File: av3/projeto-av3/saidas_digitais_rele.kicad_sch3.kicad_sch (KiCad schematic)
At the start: 0 parts

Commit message: Ligação do cristal no atmega2560 e início do esquemático das saídas digitais com relé.
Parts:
- added D9: 1N4004, Diode_THT:D_DO-41_SOD81_P10.16mm_Horizontal, symbol Diode:1N4004
- added J5: Screw_Terminal_01x03, symbol Connector:Screw_Terminal_01x03
- added K1: Relay_SPDT, symbol Relay:Relay_SPDT
- added Q1: BC337, Package_TO_SOT_THT:TO-92_Inline, symbol Transistor_BJT:BC337
- added R13: R, symbol Device:R
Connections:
- new net: J5.1 (Pin_1), K1.11
- new net: J5.2 (Pin_2), K1.14
- new net: J5.3 (Pin_3), K1.12
- new net: D9.2 (A), K1.A2, Q1.1 (C)
- new net: Q1.2 (B), R13.2
- new net +5V: D9.1 (K), K1.A1
- new net Earth: Q1.3 (E)

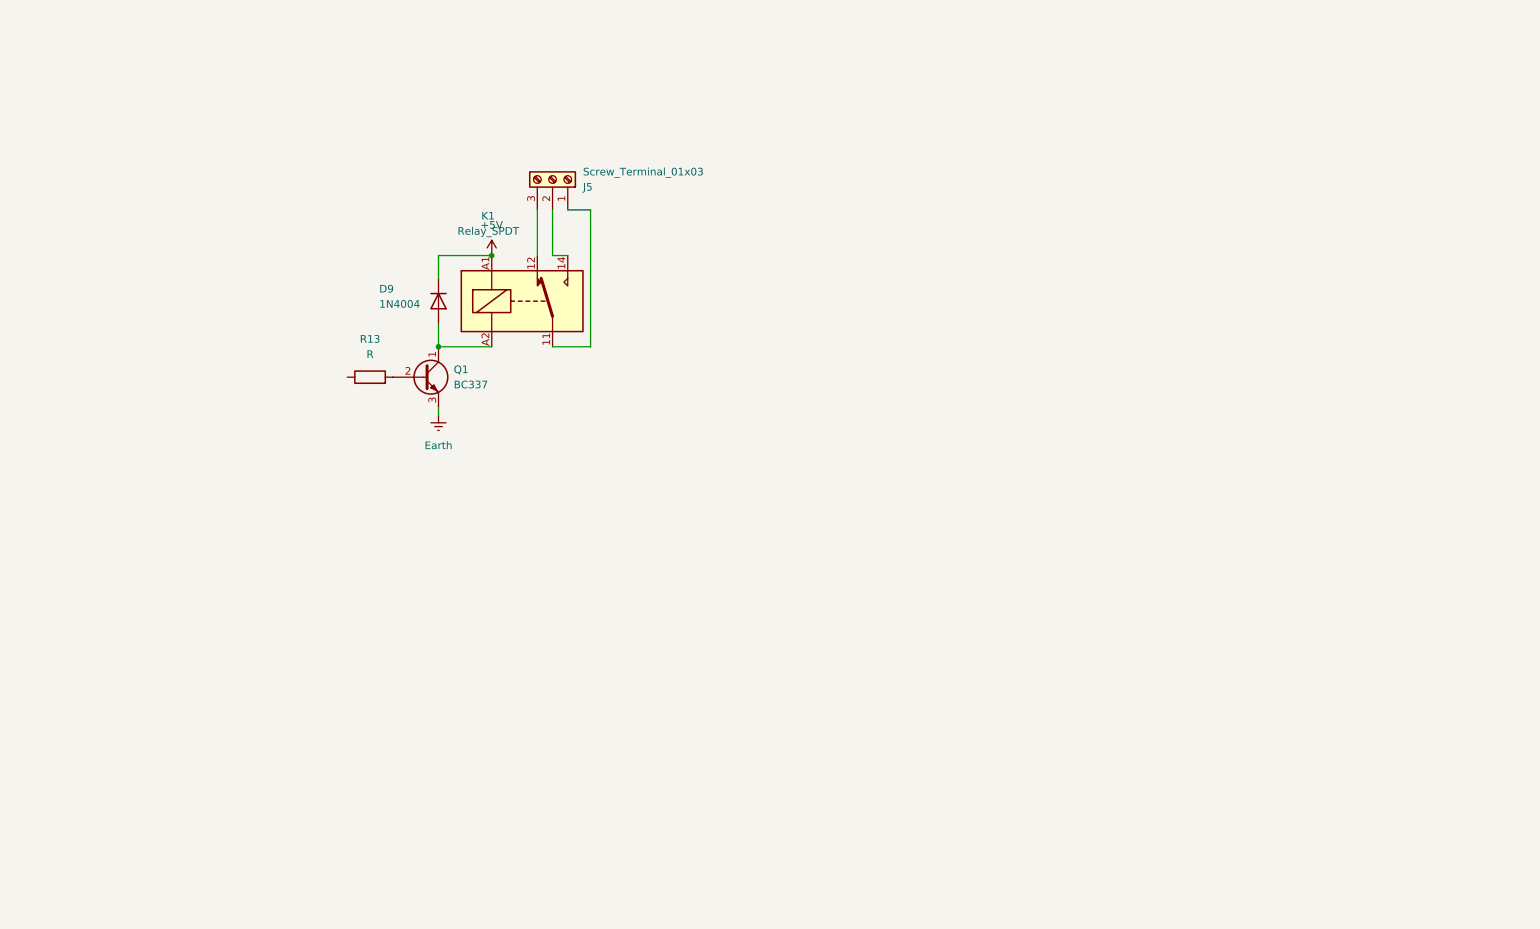
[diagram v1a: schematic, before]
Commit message: Maioria dos esquemáticos finalizados.
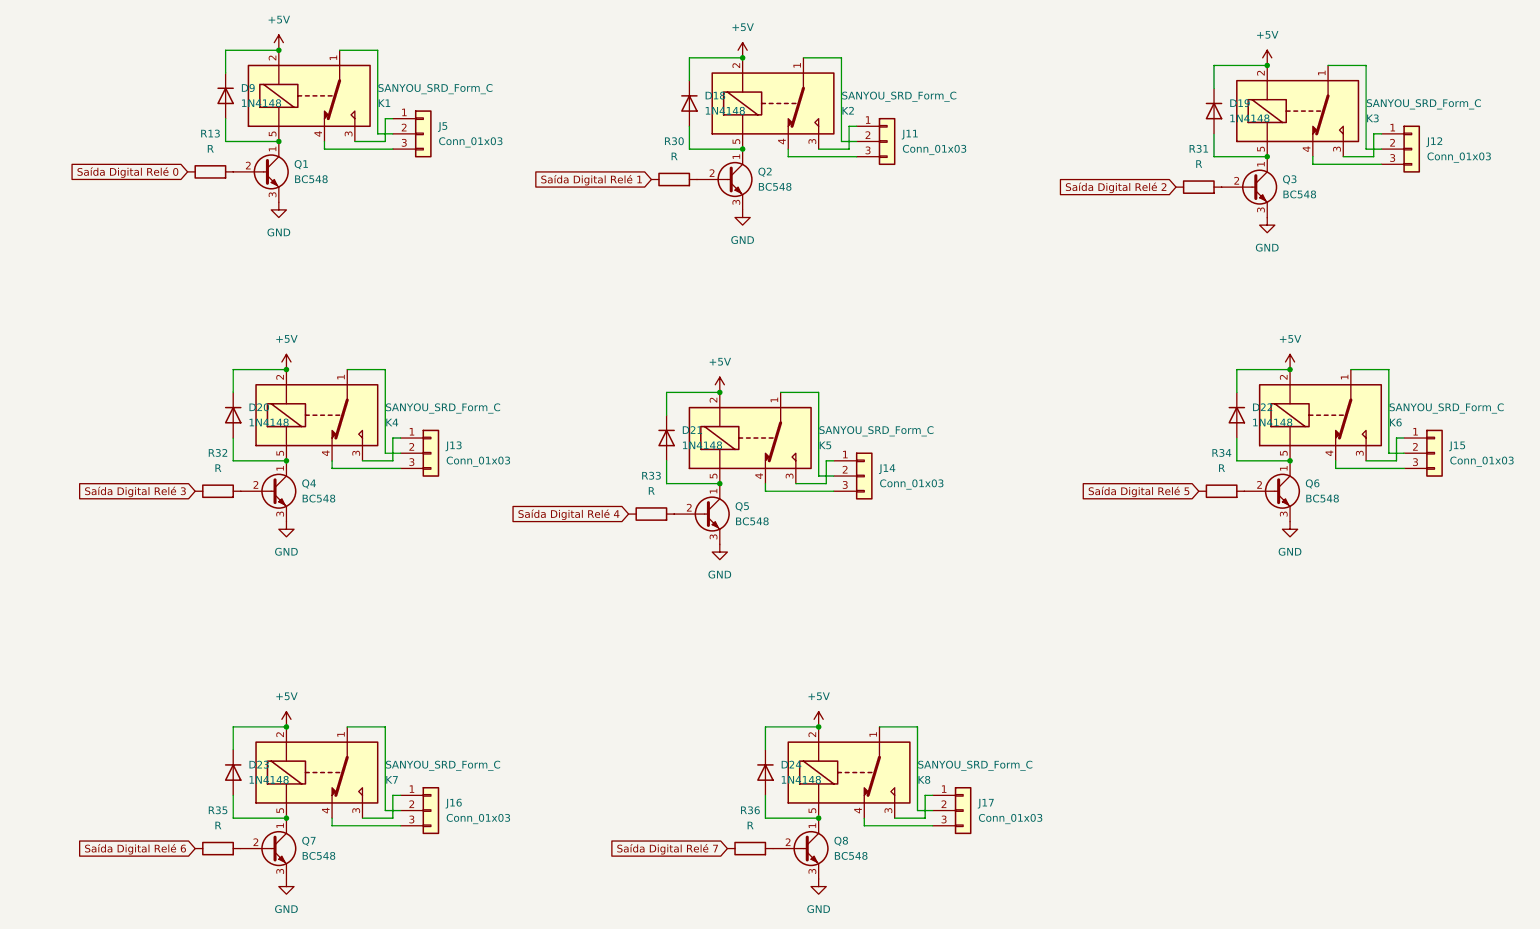
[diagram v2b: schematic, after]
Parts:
- removed D9: 1N4004, Diode_THT:D_DO-41_SOD81_P10.16mm_Horizontal, symbol Diode:1N4004
- removed J5: Screw_Terminal_01x03, symbol Connector:Screw_Terminal_01x03
- removed K1: Relay_SPDT, symbol Relay:Relay_SPDT
- removed Q1: BC337, Package_TO_SOT_THT:TO-92_Inline, symbol Transistor_BJT:BC337
- added D18, D19, D20, D21, D22, D23, D24, D9: 1N4148, Diode_THT:D_DO-35_SOD27_P7.62mm_Horizontal, symbol Diode:1N4148
- added J11, J12, J13, J14, J15, J16, J17, J5: Conn_01x03, symbol Connector_Generic:Conn_01x03
- added K1, K2, K3, K4, K5, K6, K7, K8: SANYOU_SRD_Form_C, Relay_THT:Relay_SPDT_SANYOU_SRD_Series_Form_C, symbol Relay:SANYOU_SRD_Form_C
- added Q1, Q2, Q3, Q4, Q5, Q6, Q7, Q8: BC548, Package_TO_SOT_THT:TO-92_Inline, symbol Transistor_BJT:BC548
- added R30, R31, R32, R33, R34, R35, R36: R, symbol Device:R
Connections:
- net +5V: now also D18.1 (K), D19.1 (K), D20.1 (K), D21.1 (K), D22.1 (K), D23.1 (K), D24.1 (K), D9.1 (K), K1.2, K2.2, K3.2, K4.2, K5.2, K6.2, K7.2, K8.2
- net Saída Digital Relé 0: now reaches R13.1
- net at R13.2: now also Q1.2 (B)
- new net: J13.2 (Pin_2), K4.1
- new net: J13.1 (Pin_1), K4.3
- new net: J13.3 (Pin_3), K4.4
- new net: D20.2 (A), K4.5, Q4.1 (C)
- new net: J5.2 (Pin_2), K1.1
- new net: J5.1 (Pin_1), K1.3
- new net: J5.3 (Pin_3), K1.4
- new net: D9.2 (A), K1.5, Q1.1 (C)
- new net: D24.2 (A), K8.5, Q8.1 (C)
- new net: D19.2 (A), K3.5, Q3.1 (C)
- new net: D18.2 (A), K2.5, Q2.1 (C)
- new net: Q8.2 (B), R36.2
- new net: D22.2 (A), K6.5, Q6.1 (C)
- new net: Q6.2 (B), R34.2
- new net: Q3.2 (B), R31.2
- new net: D21.2 (A), K5.5, Q5.1 (C)
- new net: Q5.2 (B), R33.2
- new net: J14.2 (Pin_2), K5.1
- new net: J14.1 (Pin_1), K5.3
- new net: J14.3 (Pin_3), K5.4
- new net: Q7.2 (B), R35.2
- new net: J15.1 (Pin_1), K6.3
- new net: J15.2 (Pin_2), K6.1
- new net: J15.3 (Pin_3), K6.4
- new net: J11.1 (Pin_1), K2.3
- new net: J11.2 (Pin_2), K2.1
- new net: J11.3 (Pin_3), K2.4
- new net: J12.2 (Pin_2), K3.1
- new net: J12.1 (Pin_1), K3.3
- new net: J12.3 (Pin_3), K3.4
- new net: J16.2 (Pin_2), K7.1
- new net: J16.1 (Pin_1), K7.3
- new net: J16.3 (Pin_3), K7.4
- new net: D23.2 (A), K7.5, Q7.1 (C)
- new net: Q2.2 (B), R30.2
- new net: J17.2 (Pin_2), K8.1
- new net: J17.1 (Pin_1), K8.3
- new net: J17.3 (Pin_3), K8.4
- new net: Q4.2 (B), R32.2
- new net GND: Q1.3 (E), Q2.3 (E), Q3.3 (E), Q4.3 (E), Q5.3 (E), Q6.3 (E), Q7.3 (E), Q8.3 (E)
- new net Saída Digital Relé 1: R30.1
- new net Saída Digital Relé 2: R31.1
- new net Saída Digital Relé 3: R32.1
- new net Saída Digital Relé 4: R33.1
- new net Saída Digital Relé 5: R34.1
- new net Saída Digital Relé 6: R35.1
- new net Saída Digital Relé 7: R36.1

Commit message: Esquemático finalizado, faltando somente o PCB.
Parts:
- J11, J12, J13, J14, J15, J16, J17, J5: footprint (none) -> TerminalBlock_Phoenix:TerminalBlock_Phoenix_MKDS-1,5-3-5.08_1x03_P5.08mm_Horizontal
- R13, R30, R31, R32, R33, R34, R35, R36: value R -> 1k; footprint (none) -> Resistor_THT:R_Axial_DIN0204_L3.6mm_D1.6mm_P5.08mm_Horizontal
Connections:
- net Saída Digital Relé 0 renamed O.0
- net Saída Digital Relé 1 renamed O.1
- net Saída Digital Relé 2 renamed O.2
- net Saída Digital Relé 3 renamed O.3
- net Saída Digital Relé 4 renamed O.4
- net Saída Digital Relé 5 renamed O.5
- net Saída Digital Relé 6 renamed O.6
- net Saída Digital Relé 7 renamed O.7
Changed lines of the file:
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@@
 		)
 	)
-	(global_label "Saída Digital Relé 6"
+	(global_label "O.6"
 		(shape input)
 		(at 43.18 156.21 180)
@@
 		)
 		(property "Intersheetrefs" "${INTERSHEET_REFS}"
-			(at 20.5403 156.21 0)
+			(at 37.05 156.21 0)
 			(effects
 				(font
@@
 		)
 	)
-	(global_label "Saída Digital Relé 4"
+	(global_label "O.4"
 		(shape input)
 		(at 115.57 100.33 180)
@@
 		)
 		(property "Intersheetrefs" "${INTERSHEET_REFS}"
-			(at 92.9303 100.33 0)
+			(at 109.44 100.33 0)
 			(effects
 				(font
@@
 		)
 	)
-	(global_label "Saída Digital Relé 2"
+	(global_label "O.2"
 		(shape input)
 		(at 207.01 45.72 180)
@@
 		)
 		(property "Intersheetrefs" "${INTERSHEET_REFS}"
-			(at 184.3703 45.72 0)
+			(at 200.88 45.72 0)
 			(effects
 				(font
@@
 		)
 	)
-	(global_label "Saída Digital Relé 0"
+	(global_label "O.0"
 		(shape input)
 		(at 41.91 43.18 180)
@@
 		)
 		(property "Intersheetrefs" "${INTERSHEET_REFS}"
-			(at 19.2703 43.18 0)
+			(at 35.78 43.18 0)
 			(effects
 				(font
@@
 		)
 	)
-	(global_label "Saída Digital Relé 1"
+	(global_label "O.1"
 		(shape input)
 		(at 119.38 44.45 180)
@@
 		)
 		(property "Intersheetrefs" "${INTERSHEET_REFS}"
-			(at 96.7403 44.45 0)
+			(at 113.25 44.45 0)
 			(effects
 				(font
@@
 		)
 	)
-	(global_label "Saída Digital Relé 5"
+	(global_label "O.5"
 		(shape input)
 		(at 210.82 96.52 180)
@@
 		)
 		(property "Intersheetrefs" "${INTERSHEET_REFS}"
-			(at 188.1803 96.52 0)
+			(at 204.69 96.52 0)
 			(effects
 				(font
@@
 		)
 	)
-	(global_label "Saída Digital Relé 3"
+	(global_label "O.3"
 		(shape input)
 		(at 43.18 96.52 180)
@@
 		)
 		(property "Intersheetrefs" "${INTERSHEET_REFS}"
-			(at 20.5403 96.52 0)
+			(at 37.05 96.52 0)
 			(effects
 				(font
@@
 		)
 	)
-	(global_label "Saída Digital Relé 7"
+	(global_label "O.7"
 		(shape input)
 		(at 132.08 156.21 180)
@@
 		)
 		(property "Intersheetrefs" "${INTERSHEET_REFS}"
-			(at 109.4403 156.21 0)
+			(at 125.95 156.21 0)
 			(effects
 				(font
@@
 			)
 		)
-		(property "Value" "R"
+		(property "Value" "1k"
 			(at 135.89 152.4 90)
 			(effects
@@
 			)
 		)
-		(property "Footprint" ""
+		(property "Footprint" "Resistor_THT:R_Axial_DIN0204_L3.6mm_D1.6mm_P5.08mm_Horizontal"
 			(at 135.89 157.988 90)
 			(effects
@@
 			)
 		)
-		(property "Value" "R"
+		(property "Value" "1k"
 			(at 45.72 39.37 90)
 			(effects
@@
 			)
 		)
-		(property "Footprint" ""
+		(property "Footprint" "Resistor_THT:R_Axial_DIN0204_L3.6mm_D1.6mm_P5.08mm_Horizontal"
 			(at 45.72 44.958 90)
 			(effects
@@
 			)
 		)
-		(property "Footprint" ""
+		(property "Footprint" "TerminalBlock_Phoenix:TerminalBlock_Phoenix_MKDS-1,5-3-5.08_1x03_P5.08mm_Horizontal"
 			(at 82.55 90.17 0)
 			(effects
@@
 			)
 		)
-		(property "Value" "R"
+		(property "Value" "1k"
 			(at 210.82 41.91 90)
 			(effects
@@
 			)
 		)
-		(property "Footprint" ""
+		(property "Footprint" "Resistor_THT:R_Axial_DIN0204_L3.6mm_D1.6mm_P5.08mm_Horizontal"
 			(at 210.82 47.498 90)
 			(effects
@@
 			)
 		)
-		(property "Value" "R"
+		(property "Value" "1k"
 			(at 46.99 152.4 90)
 			(effects
@@
 			)
 		)
-		(property "Footprint" ""
+		(property "Footprint" "Resistor_THT:R_Axial_DIN0204_L3.6mm_D1.6mm_P5.08mm_Horizontal"
 			(at 46.99 157.988 90)
 			(effects
@@
 			)
 		)
-		(property "Footprint" ""
+		(property "Footprint" "TerminalBlock_Phoenix:TerminalBlock_Phoenix_MKDS-1,5-3-5.08_1x03_P5.08mm_Horizontal"
 			(at 250.19 90.17 0)
 			(effects
@@
 			)
 		)
-		(property "Footprint" ""
+		(property "Footprint" "TerminalBlock_Phoenix:TerminalBlock_Phoenix_MKDS-1,5-3-5.08_1x03_P5.08mm_Horizontal"
 			(at 158.75 38.1 0)
 			(effects
@@
 			)
 		)
-		(property "Footprint" ""
+		(property "Footprint" "TerminalBlock_Phoenix:TerminalBlock_Phoenix_MKDS-1,5-3-5.08_1x03_P5.08mm_Horizontal"
 			(at 154.94 93.98 0)
 			(effects
@@
 			)
 		)
-		(property "Footprint" ""
+		(property "Footprint" "TerminalBlock_Phoenix:TerminalBlock_Phoenix_MKDS-1,5-3-5.08_1x03_P5.08mm_Horizontal"
 			(at 246.38 39.37 0)
 			(effects
@@
 			)
 		)
-		(property "Value" "R"
+		(property "Value" "1k"
 			(at 214.63 92.71 90)
 			(effects
@@
 			)
 		)
-		(property "Footprint" ""
+		(property "Footprint" "Resistor_THT:R_Axial_DIN0204_L3.6mm_D1.6mm_P5.08mm_Horizontal"
 			(at 214.63 98.298 90)
 			(effects
@@
 			)
 		)
-		(property "Value" "R"
+		(property "Value" "1k"
 			(at 119.38 96.52 90)
 			(effects
@@
 			)
 		)
-		(property "Footprint" ""
+		(property "Footprint" "Resistor_THT:R_Axial_DIN0204_L3.6mm_D1.6mm_P5.08mm_Horizontal"
 			(at 119.38 102.108 90)
 			(effects
@@
 			)
 		)
-		(property "Value" "R"
+		(property "Value" "1k"
 			(at 46.99 92.71 90)
 			(effects
@@
 			)
 		)
-		(property "Footprint" ""
+		(property "Footprint" "Resistor_THT:R_Axial_DIN0204_L3.6mm_D1.6mm_P5.08mm_Horizontal"
 			(at 46.99 98.298 90)
 			(effects
@@
 			)
 		)
-		(property "Value" "R"
+		(property "Value" "1k"
 			(at 123.19 40.64 90)
 			(effects
@@
 			)
 		)
-		(property "Footprint" ""
+		(property "Footprint" "Resistor_THT:R_Axial_DIN0204_L3.6mm_D1.6mm_P5.08mm_Horizontal"
 			(at 123.19 46.228 90)
 			(effects
@@
 			)
 		)
-		(property "Footprint" ""
+		(property "Footprint" "TerminalBlock_Phoenix:TerminalBlock_Phoenix_MKDS-1,5-3-5.08_1x03_P5.08mm_Horizontal"
 			(at 82.55 149.86 0)
 			(effects
@@
 			)
 		)
-		(property "Footprint" ""
+		(property "Footprint" "TerminalBlock_Phoenix:TerminalBlock_Phoenix_MKDS-1,5-3-5.08_1x03_P5.08mm_Horizontal"
 			(at 81.28 36.83 0)
 			(effects
@@
 			)
 		)
-		(property "Footprint" ""
+		(property "Footprint" "TerminalBlock_Phoenix:TerminalBlock_Phoenix_MKDS-1,5-3-5.08_1x03_P5.08mm_Horizontal"
 			(at 171.45 149.86 0)
 			(effects

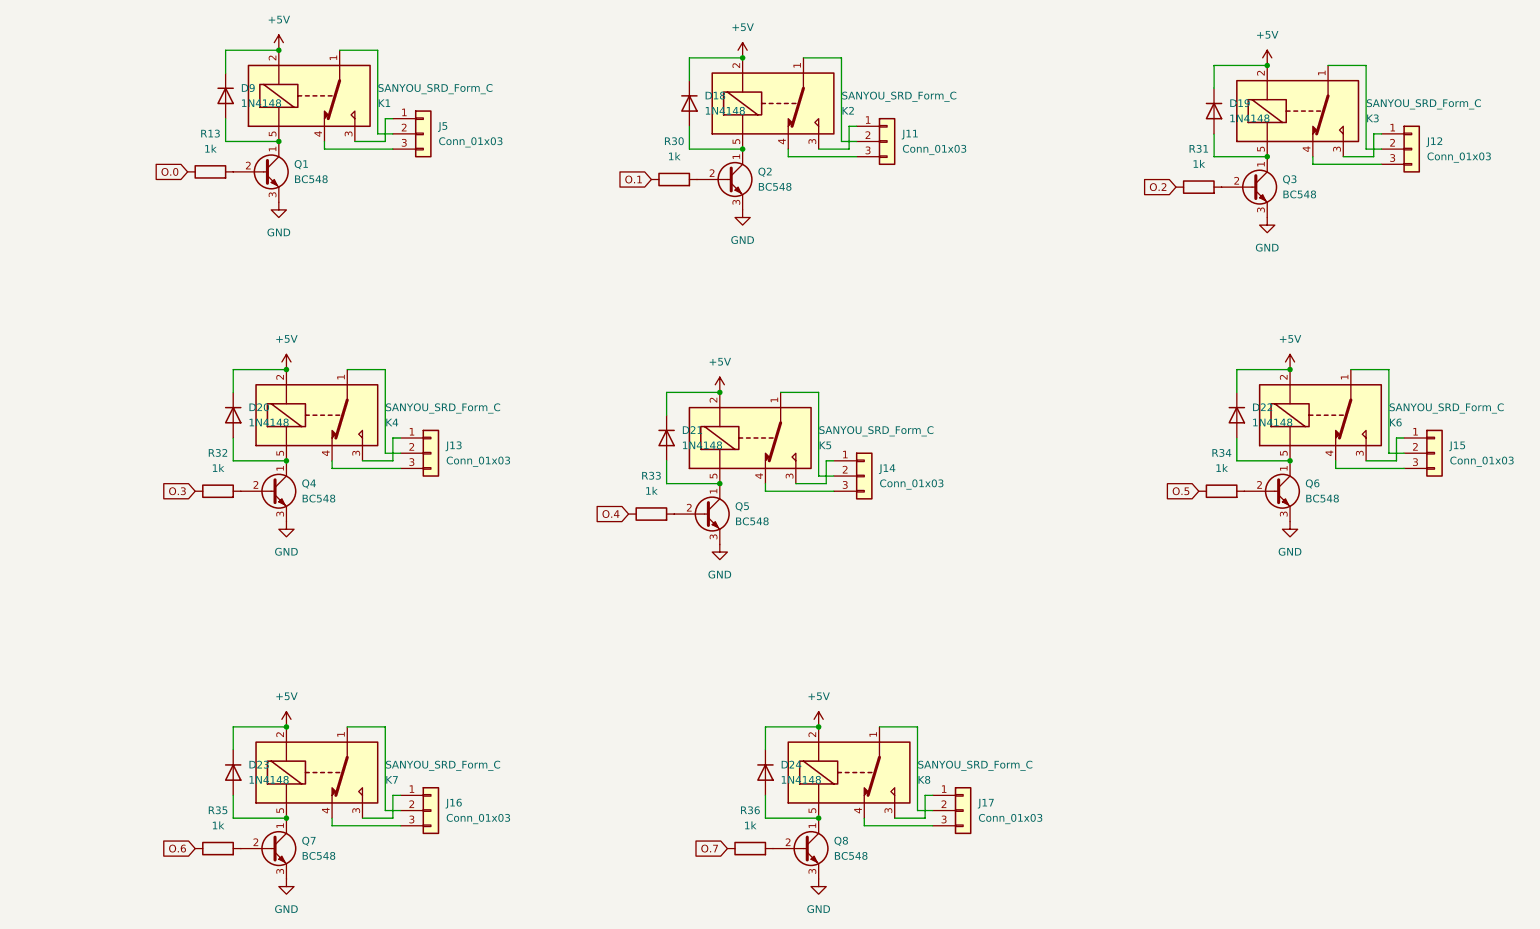
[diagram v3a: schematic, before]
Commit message: Referencias de componentes resetados; Progresso de 20% no PCB;
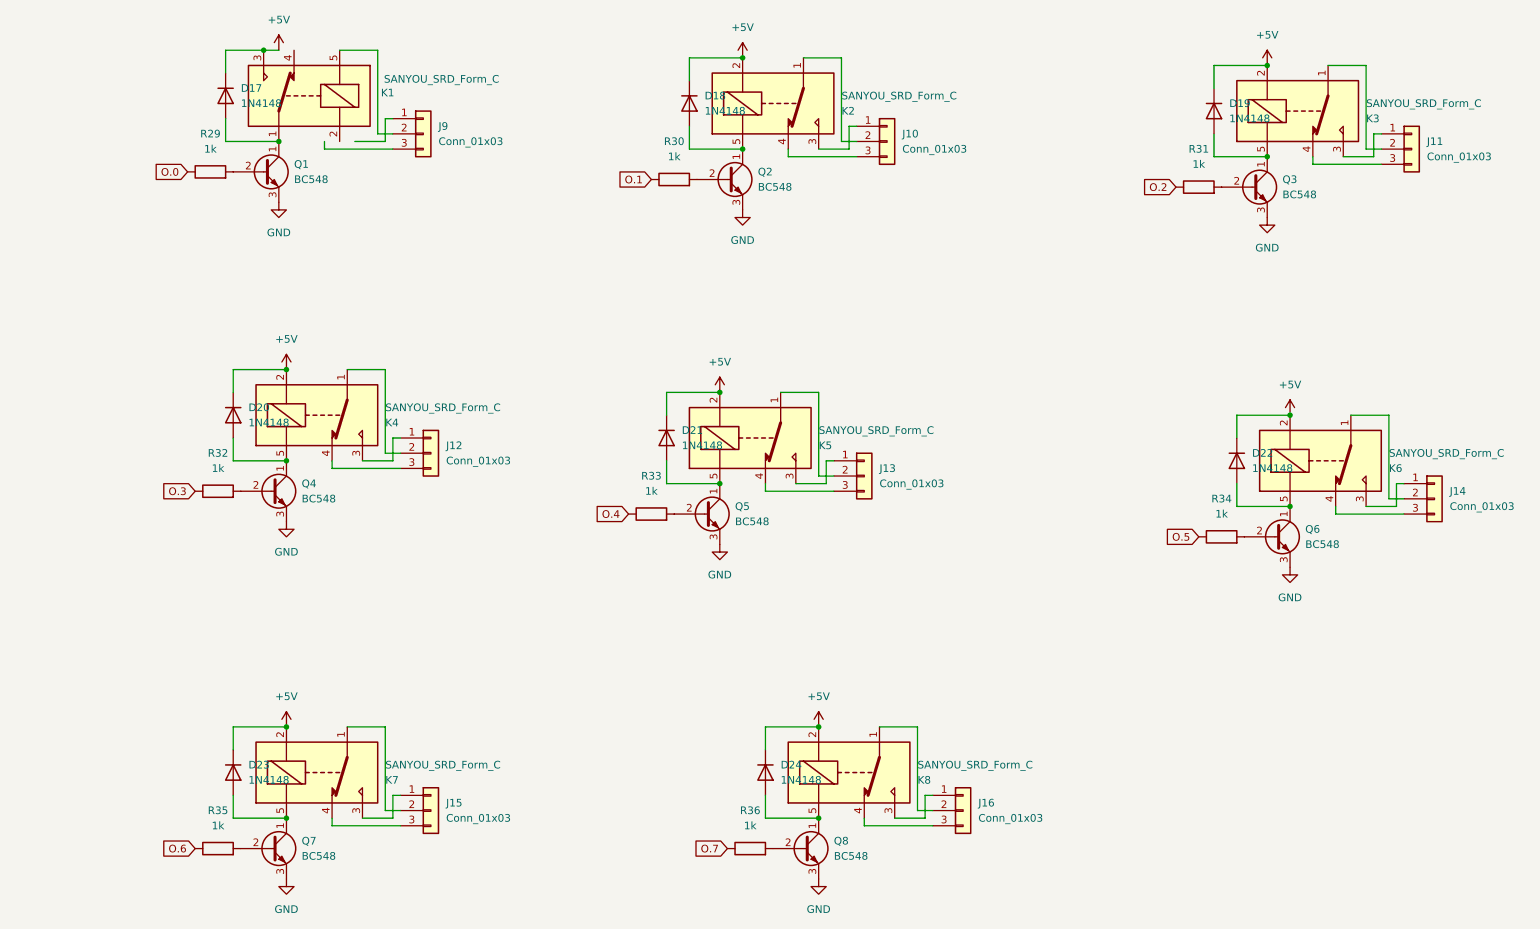
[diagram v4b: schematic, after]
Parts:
- renumbered D9 to D17, J11 to J10, J12 to J11, J13 to J12, J14 to J13, J15 to J14, J16 to J15, J17 to J16, J5 to J9, R13 to R29
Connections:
- net +5V: now also K1.3; no longer K1.2
- net at K1.1: now also D17.2 (A), Q1.1 (C); no longer J9.2 (Pin_2)
- net at J9.1 (Pin_1): no longer K1.3
- net at K1.4: no longer J9.3 (Pin_3)
- new net: J9.2 (Pin_2), K1.5
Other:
- moved on the sheet: D22, J14, K6, Q6, R34
